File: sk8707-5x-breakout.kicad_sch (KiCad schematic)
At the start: 8 parts, among them J1 Conn_01x08_Socket, J2 Conn_01x04_Pin

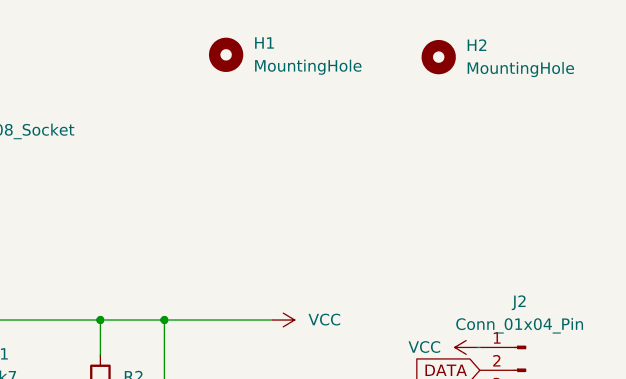
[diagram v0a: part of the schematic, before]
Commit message: edited routing and grounded mounting holes
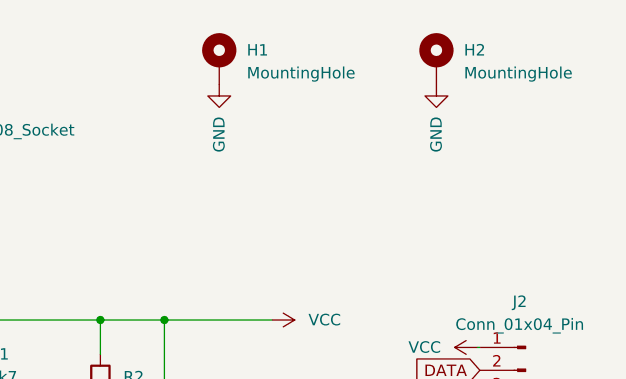
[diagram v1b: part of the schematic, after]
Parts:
- H1, H2: footprint MountingHole:MountingHole_2.2mm_M2 -> MountingHole:MountingHole_2.2mm_M2_Pad; symbol Mechanical:MountingHole -> Mechanical:MountingHole_Pad
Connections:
- net GND: now also H1.1, H2.1
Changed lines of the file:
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@@
+    )
+  )
+  (symbol (lib_id "power:GND") (at 105.41 36.83 0) (mirror y) (unit 1)
+    (in_bom yes) (on_board yes) (dnp no)
+    (property "Reference" "#PWR05" (at 105.41 43.18 0)
+      (effects (font (size 1.27 1.27)) hide)
+    )
+    (property "Value" "GND" (at 105.41 40.386 90)
+      (effects (font (size 1.27 1.27)) (justify right))
+    )
+    (property "Footprint" "" (at 105.41 36.83 0)
+      (effects (font (size 1.27 1.27)) hide)
+    )
+    (property "Datasheet" "" (at 105.41 36.83 0)
+      (effects (font (size 1.27 1.27)) hide)
+    )
+    (pin "1")
+    (instances
+      (project "sk8707-5x-breakout"
+        (path "/be558a7b-33de-4f14-a66b-c653182f9243"
+          (reference "#PWR05") (unit 1)
+        )
+      )
     )
   )
@@
     )
   )
-  (symbol (lib_id "Mechanical:MountingHole") (at 106.172 33.528 0) (unit 1)
-    (in_bom yes) (on_board yes) (dnp no) (fields_autoplaced)
-    (property "Reference" "H1" (at 109.22 32.258 0)
-      (effects (font (size 1.27 1.27)) (justify left))
-    )
-    (property "Value" "MountingHole" (at 109.22 34.798 0)
-      (effects (font (size 1.27 1.27)) (justify left))
-    )
-    (property "Footprint" "MountingHole:MountingHole_2.2mm_M2" (at 106.172 33.528 0)
-      (effects (font (size 1.27 1.27)) hide)
-    )
-    (property "Datasheet" "~" (at 106.172 33.528 0)
-      (effects (font (size 1.27 1.27)) hide)
-    )
+  (symbol (lib_id "Mechanical:MountingHole_Pad") (at 105.41 34.29 0) (unit 1)
+    (in_bom yes) (on_board yes) (dnp no) (fields_autoplaced)
+    (property "Reference" "H1" (at 108.458 33.02 0)
+      (effects (font (size 1.27 1.27)) (justify left))
+    )
+    (property "Value" "MountingHole" (at 108.458 35.56 0)
+      (effects (font (size 1.27 1.27)) (justify left))
+    )
+    (property "Footprint" "MountingHole:MountingHole_2.2mm_M2_Pad" (at 105.41 34.29 0)
+      (effects (font (size 1.27 1.27)) hide)
+    )
+    (property "Datasheet" "~" (at 105.41 34.29 0)
+      (effects (font (size 1.27 1.27)) hide)
+    )
+    (pin "1")
     (instances
       (project "sk8707-5x-breakout"
@@
     )
   )
-  (symbol (lib_id "Mechanical:MountingHole") (at 129.794 33.782 0) (unit 1)
-    (in_bom yes) (on_board yes) (dnp no) (fields_autoplaced)
-    (property "Reference" "H2" (at 132.842 32.512 0)
-      (effects (font (size 1.27 1.27)) (justify left))
-    )
-    (property "Value" "MountingHole" (at 132.842 35.052 0)
-      (effects (font (size 1.27 1.27)) (justify left))
-    )
-    (property "Footprint" "MountingHole:MountingHole_2.2mm_M2" (at 129.794 33.782 0)
-      (effects (font (size 1.27 1.27)) hide)
-    )
-    (property "Datasheet" "~" (at 129.794 33.782 0)
-      (effects (font (size 1.27 1.27)) hide)
-    )
+  (symbol (lib_id "Mechanical:MountingHole_Pad") (at 129.54 34.29 0) (unit 1)
+    (in_bom yes) (on_board yes) (dnp no) (fields_autoplaced)
+    (property "Reference" "H2" (at 132.588 33.02 0)
+      (effects (font (size 1.27 1.27)) (justify left))
+    )
+    (property "Value" "MountingHole" (at 132.588 35.56 0)
+      (effects (font (size 1.27 1.27)) (justify left))
+    )
+    (property "Footprint" "MountingHole:MountingHole_2.2mm_M2_Pad" (at 129.54 34.29 0)
+      (effects (font (size 1.27 1.27)) hide)
+    )
+    (property "Datasheet" "~" (at 129.54 34.29 0)
+      (effects (font (size 1.27 1.27)) hide)
+    )
+    (pin "1")
     (instances
       (project "sk8707-5x-breakout"
@@
         )
       )
+    )
+  )
+  (symbol (lib_id "power:GND") (at 129.54 36.83 0) (mirror y) (unit 1)
+    (in_bom yes) (on_board yes) (dnp no)
+    (property "Reference" "#PWR06" (at 129.54 43.18 0)
+      (effects (font (size 1.27 1.27)) hide)
+    )
+    (property "Value" "GND" (at 129.54 40.386 90)
+      (effects (font (size 1.27 1.27)) (justify right))
+    )
+    (property "Footprint" "" (at 129.54 36.83 0)
+      (effects (font (size 1.27 1.27)) hide)
+    )
+    (property "Datasheet" "" (at 129.54 36.83 0)
+      (effects (font (size 1.27 1.27)) hide)
+    )
+    (pin "1")
+    (instances
+      (project "sk8707-5x-breakout"
+        (path "/be558a7b-33de-4f14-a66b-c653182f9243"
+          (reference "#PWR06") (unit 1)
+        )
+      )

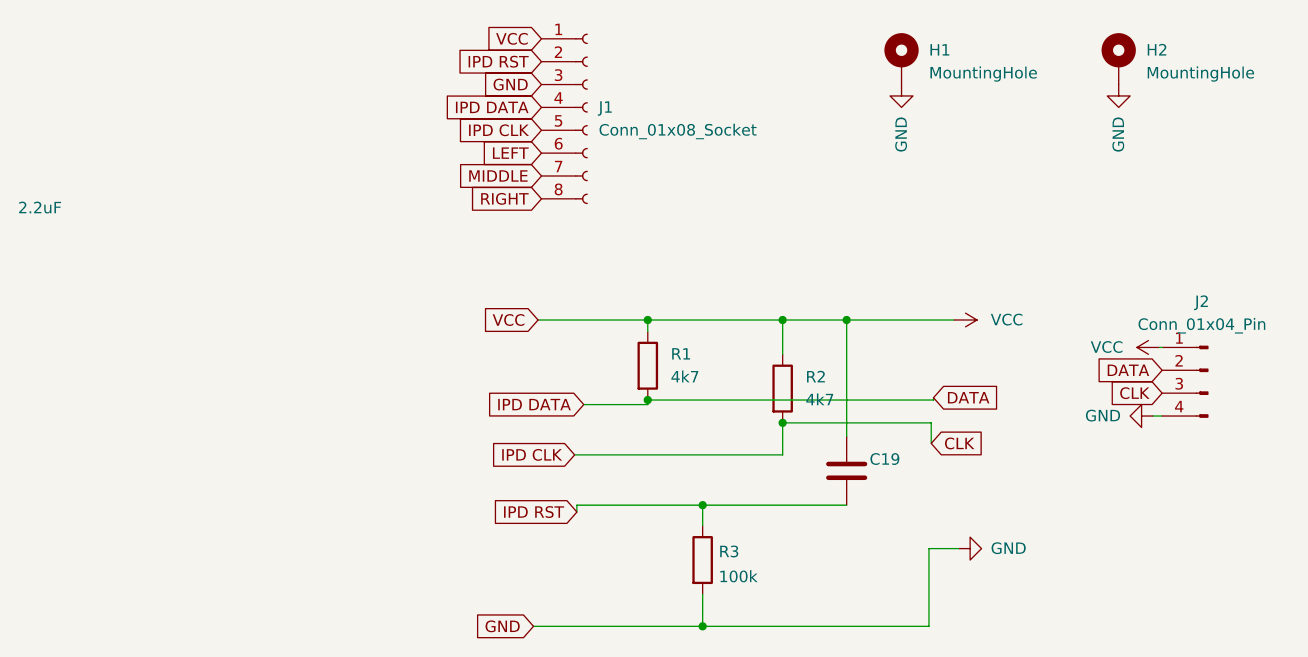
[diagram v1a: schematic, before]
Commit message: reversed pin order and grounded ffc connector
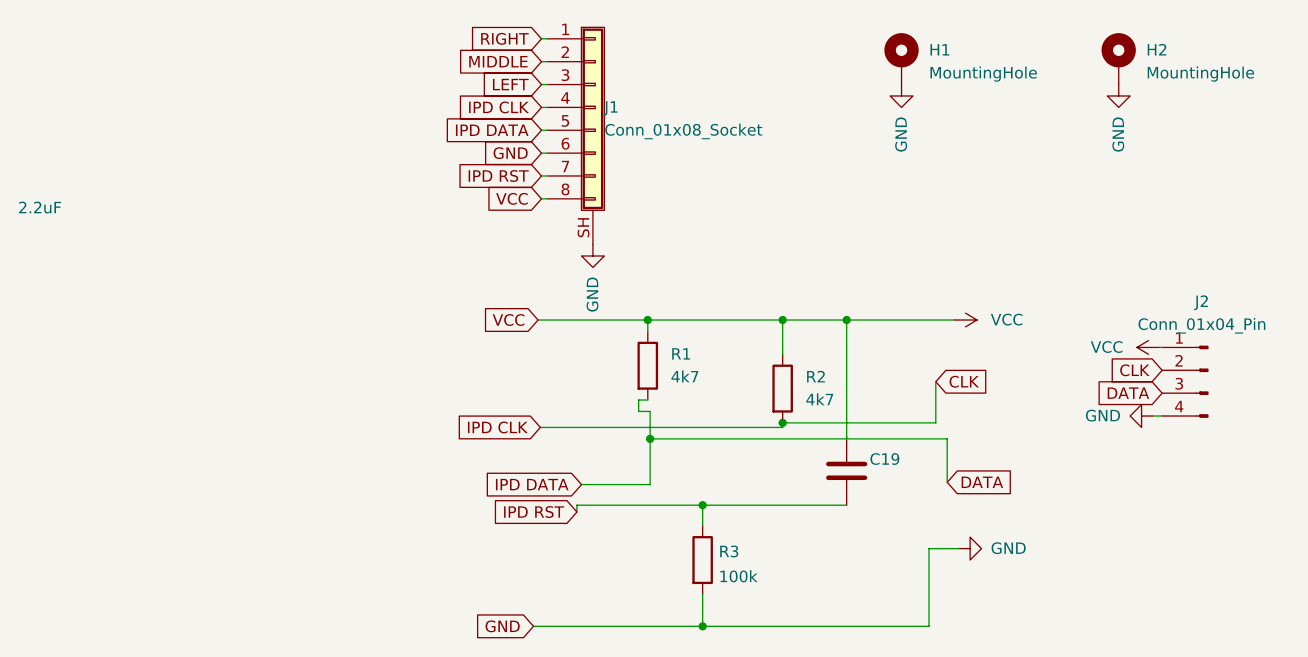
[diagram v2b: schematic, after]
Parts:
- J1: symbol Connector:Conn_01x08_Socket -> Connector_Generic_Shielded:Conn_01x08_Shielded
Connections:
- net CLK: now also J1.4 (Pin_4), J2.2 (Pin_2); no longer J1.5 (Pin_5), J2.3 (Pin_3)
- net DATA: now also J1.5 (Pin_5), J2.3 (Pin_3); no longer J1.4 (Pin_4), J2.2 (Pin_2)
- net GND: now also J1.6 (Pin_6), J1.SH (Shield); no longer J1.3 (Pin_3)
- net IPD RST: now also J1.7 (Pin_7); no longer J1.2 (Pin_2)
- net LEFT: now also J1.3 (Pin_3); no longer J1.6 (Pin_6)
- net MIDDLE: now also J1.2 (Pin_2); no longer J1.7 (Pin_7)
- net RIGHT: now also J1.1 (Pin_1); no longer J1.8 (Pin_8)
- net VCC: now also J1.8 (Pin_8); no longer J1.1 (Pin_1)
